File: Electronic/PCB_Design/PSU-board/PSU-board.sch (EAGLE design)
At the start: 7 parts

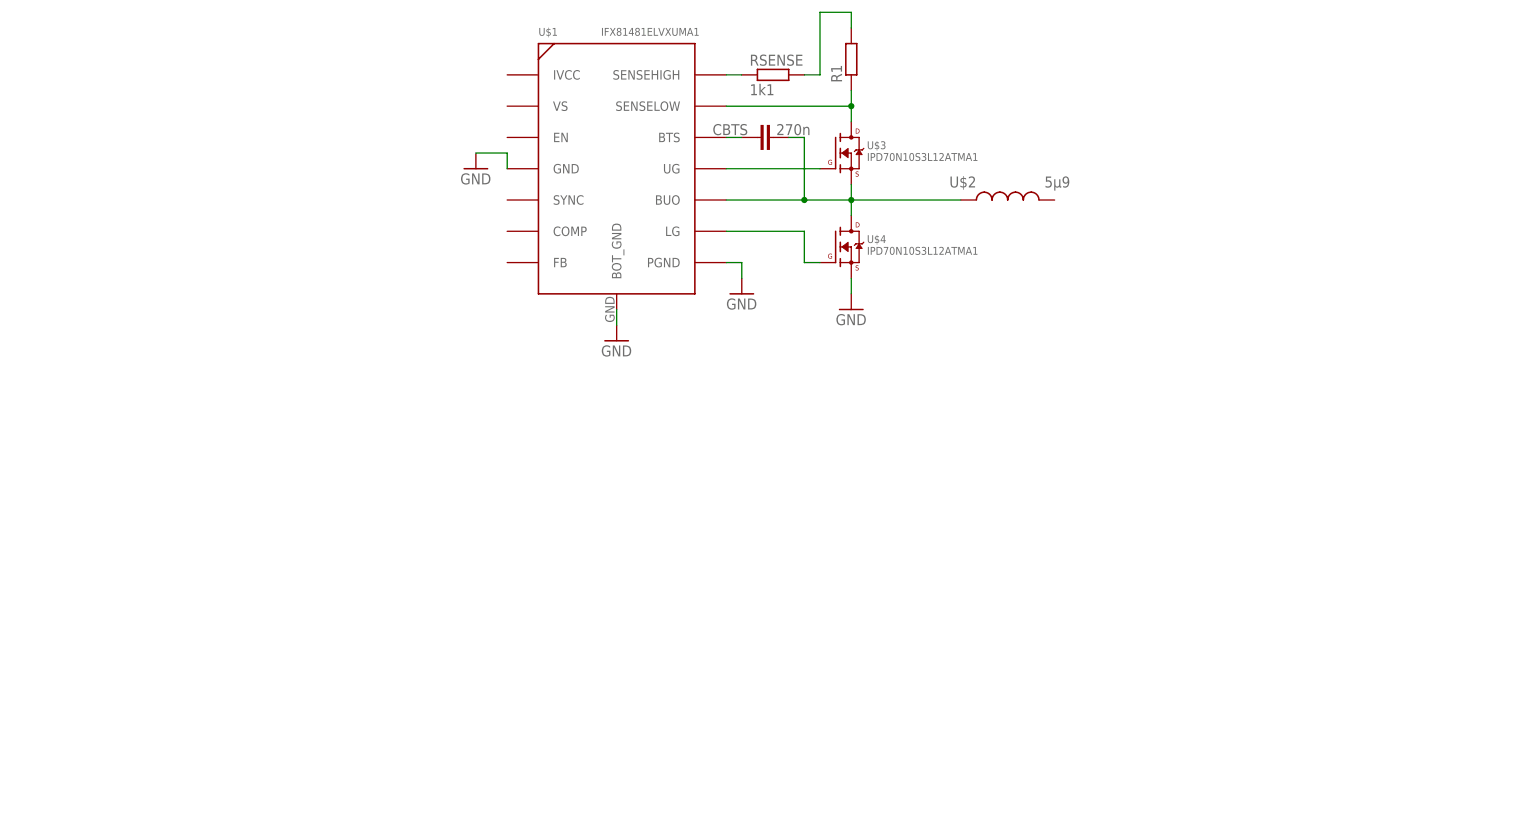
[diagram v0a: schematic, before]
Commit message: PSU schematic mandatory functionality done
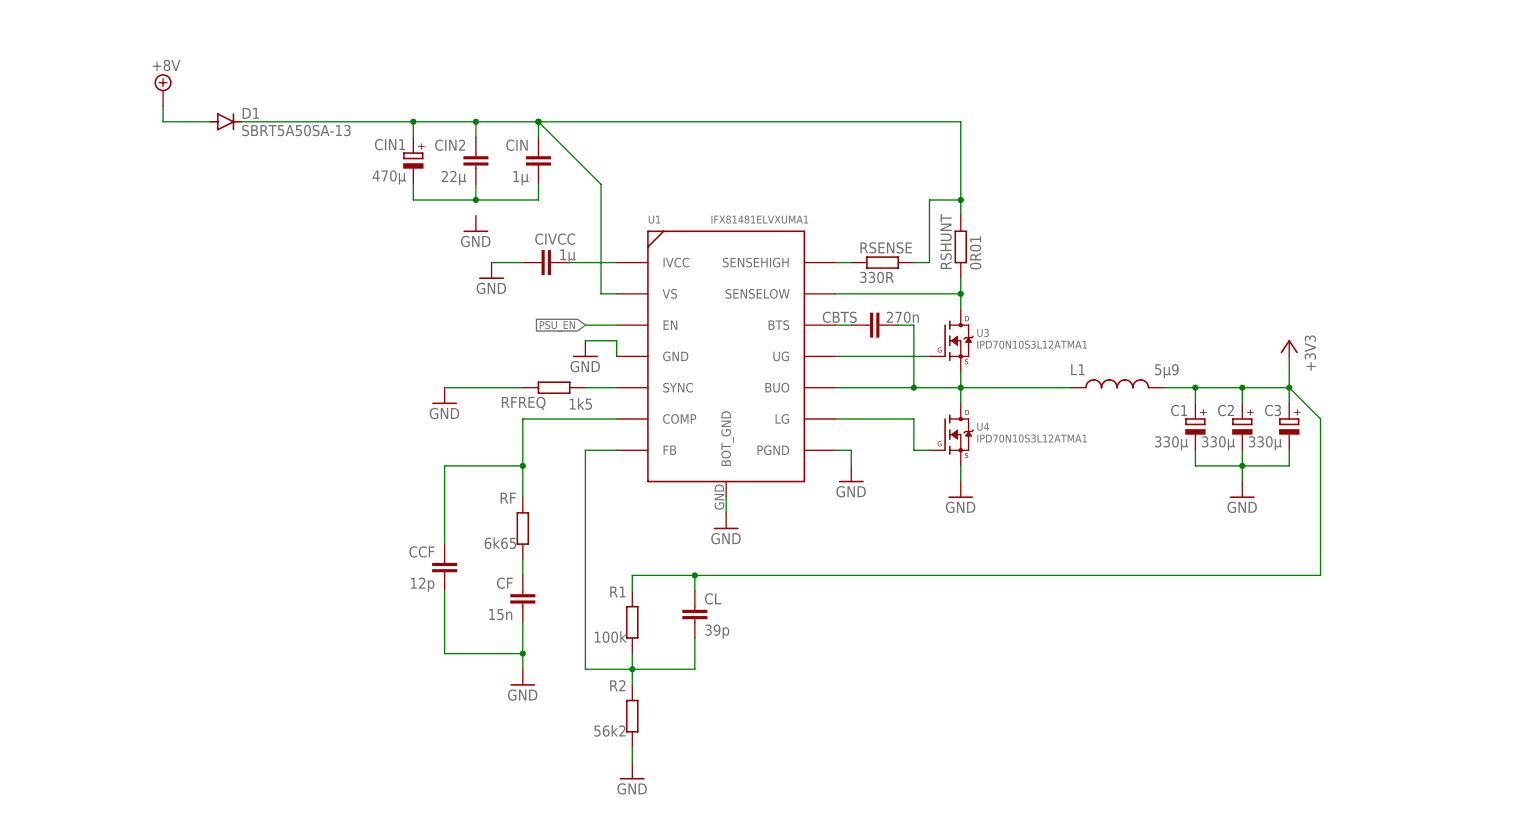
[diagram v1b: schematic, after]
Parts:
- removed U$1: IFX81481ELVXUMA1, PROPULSE:IFX81481ELVXUMA1
- removed U$2: 5µ9, PROPULSE:SRR1260A-5R6Y
- removed U$3, U$4: IPD70N10S3L12ATMA1, PROPULSE:IPD70N10S3L12ATMA1
- added C1, C2, C3: 330µ, rcl:CPOL-EUCT7343
- added CCF: 12p, rcl:C-EUC0603
- added CF: 15n, rcl:C-EUC0603
- added CIN, CIVCC: 1µ, rcl:C-EUC1206
- added CIN1: 470µ, rcl:CPOL-EUG
- added CIN2: 22µ, rcl:C-EUC2220K
- added CL: 39p, rcl:C-EUC0603
- added D1: SBRT5A50SA-13, diode:DIODE-DO214AC
- added L1: 5µ9, PROPULSE:SRR1260A-5R6Y
- added R2: 56k2, rcl:R-EU_R0603
- added RF: 6k65, rcl:R-EU_R0603
- added RFREQ: 1k5, rcl:R-EU_R0603
- added RSHUNT: 0R01, rcl:R-EU_R2512
- added U1: IFX81481ELVXUMA1, PROPULSE:IFX81481ELVXUMA1
- added U3, U4: IPD70N10S3L12ATMA1, PROPULSE:IPD70N10S3L12ATMA1
- R1: value (none) -> 100k; device rcl:R-EU_R2512 -> rcl:R-EU_R0603
- RSENSE: value 1k1 -> 330R
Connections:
- removed net N$7: R1.2, RSENSE.2
- new net +3V3: C1.+, C2.+, C3.+, CL.1, L1.2, R1.1
- new net +8V: D1.A
- new net N$11: CL.2, R1.2, R2.1, U1.FB
- new net N$12: CIN.1, CIN1.+, CIN2.1, D1.C, RSENSE.2, RSHUNT.2, U1.VS
- new net N$13: CCF.1, RF.1, U1.COMP
- new net N$14: CIN.2, CIN1.-, CIN2.2
- new net N$15: CF.1, RF.2
- new net N$8: RFREQ.1, U1.SYNC
- new net N$9: CIVCC.2, U1.IVCC
- new net PSU_EN: U1.EN
- net GND: now also C1.-, C2.-, C3.-, CCF.2, CF.2, CIVCC.1, R2.2, RFREQ.2, U1.BOT_GND, U1.GND, U1.PGND, U4.S; no longer U$1.BOT_GND, U$1.GND, U$1.PGND, U$4.S
- net N$1: now also L1.1, U1.BUO, U3.S, U4.D; no longer U$1.BUO, U$2.1, U$3.S, U$4.D
- net N$2: now also U1.UG, U3.G; no longer U$1.UG, U$3.G
- net N$3: now also U1.LG, U4.G; no longer U$1.LG, U$4.G
- net N$4: now also U1.BTS; no longer U$1.BTS
- net N$5: now also U1.SENSEHIGH; no longer U$1.SENSEHIGH
- net N$6: now also RSHUNT.1, U1.SENSELOW, U3.D; no longer R1.1, U$1.SENSELOW, U$3.D
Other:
- moved on the sheet: CBTS, R1, RSENSE

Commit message: Added arming/disarming scetch and increased power
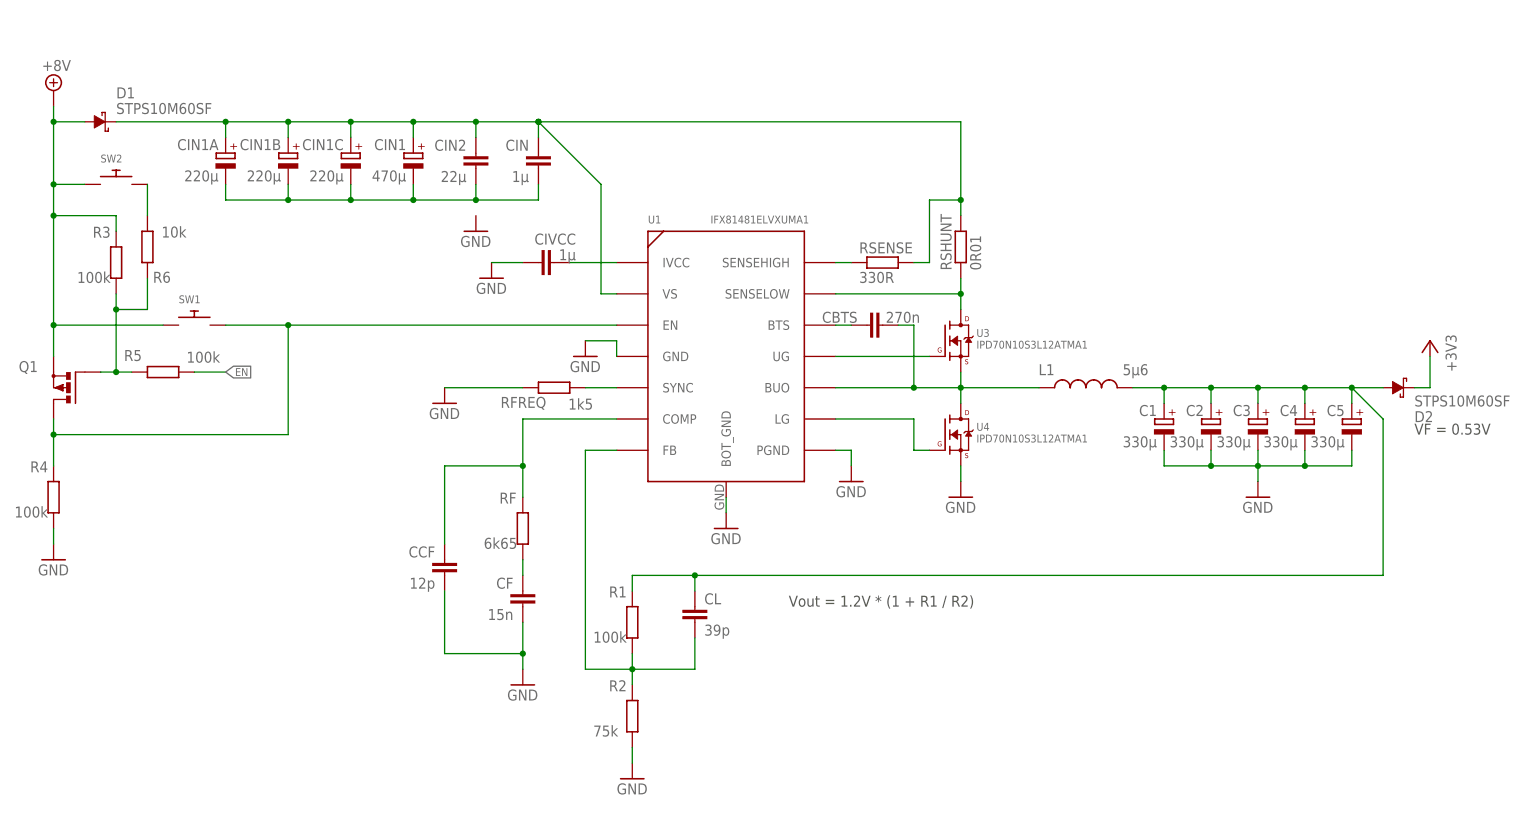
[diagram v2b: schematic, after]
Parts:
- added C4, C5: 330µ, rcl:CPOL-EUCT7343
- added CIN1A, CIN1B, CIN1C: 220µ, rcl:CPOL-EUSMCD
- added D2: STPS10M60SF, PROPULSE:STPS10M60SF
- added Q1: (no value), transistor-power:P-MOSFET-SO8
- added R3, R4, R5: 100k, rcl:R-EU_R0603
- added R6: 10k, rcl:R-EU_R0603
- added SW1, SW2: (no value), adafruit:SWITCH_PUSHBUTTONC&K_KSS
- D1: value SBRT5A50SA-13 -> STPS10M60SF; device diode:DIODE-DO214AC -> PROPULSE:STPS10M60SF
- L1: value 5µ9 -> 5µ6; device PROPULSE:SRR1260A-5R6Y -> PROPULSE:SRR1280-5R6Y
- R2: value 56k2 -> 75k
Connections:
- new net EN: R5.2
- new net N$16: R6.2, SW2.P$2
- new net N$17: Q1.G, R3.2, R5.1, R6.1
- new net N$7: C1.+, C2.+, C3.+, C4.+, C5.+, CL.1, D2.A, L1.2, R1.1
- net +3V3: now also D2.C; no longer C1.+, C2.+, C3.+, CL.1, L1.2, R1.1
- net +8V: now also Q1.S, R3.1, SW1.P$1, SW2.P$1
- net GND: now also C4.-, C5.-, R4.2
- net N$12: now also CIN1A.+, CIN1B.+, CIN1C.+
- net N$14: now also CIN1A.-, CIN1B.-, CIN1C.-
- net PSU_EN: now also Q1.D, R4.1, SW1.P$2
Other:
- note added: "VF = 0.53V"
- note added: "Vout = 1.2V * (1 + R1 / R2)"
- moved on the sheet: C1, C2, C3, L1
